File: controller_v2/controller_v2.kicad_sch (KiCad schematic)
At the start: 22 parts, among them J1 Conn_01x03_Socket, J2 WAGO 236-402, J3 WAGO 236-402, J4 WAGO 236-404, Q1 2N2222

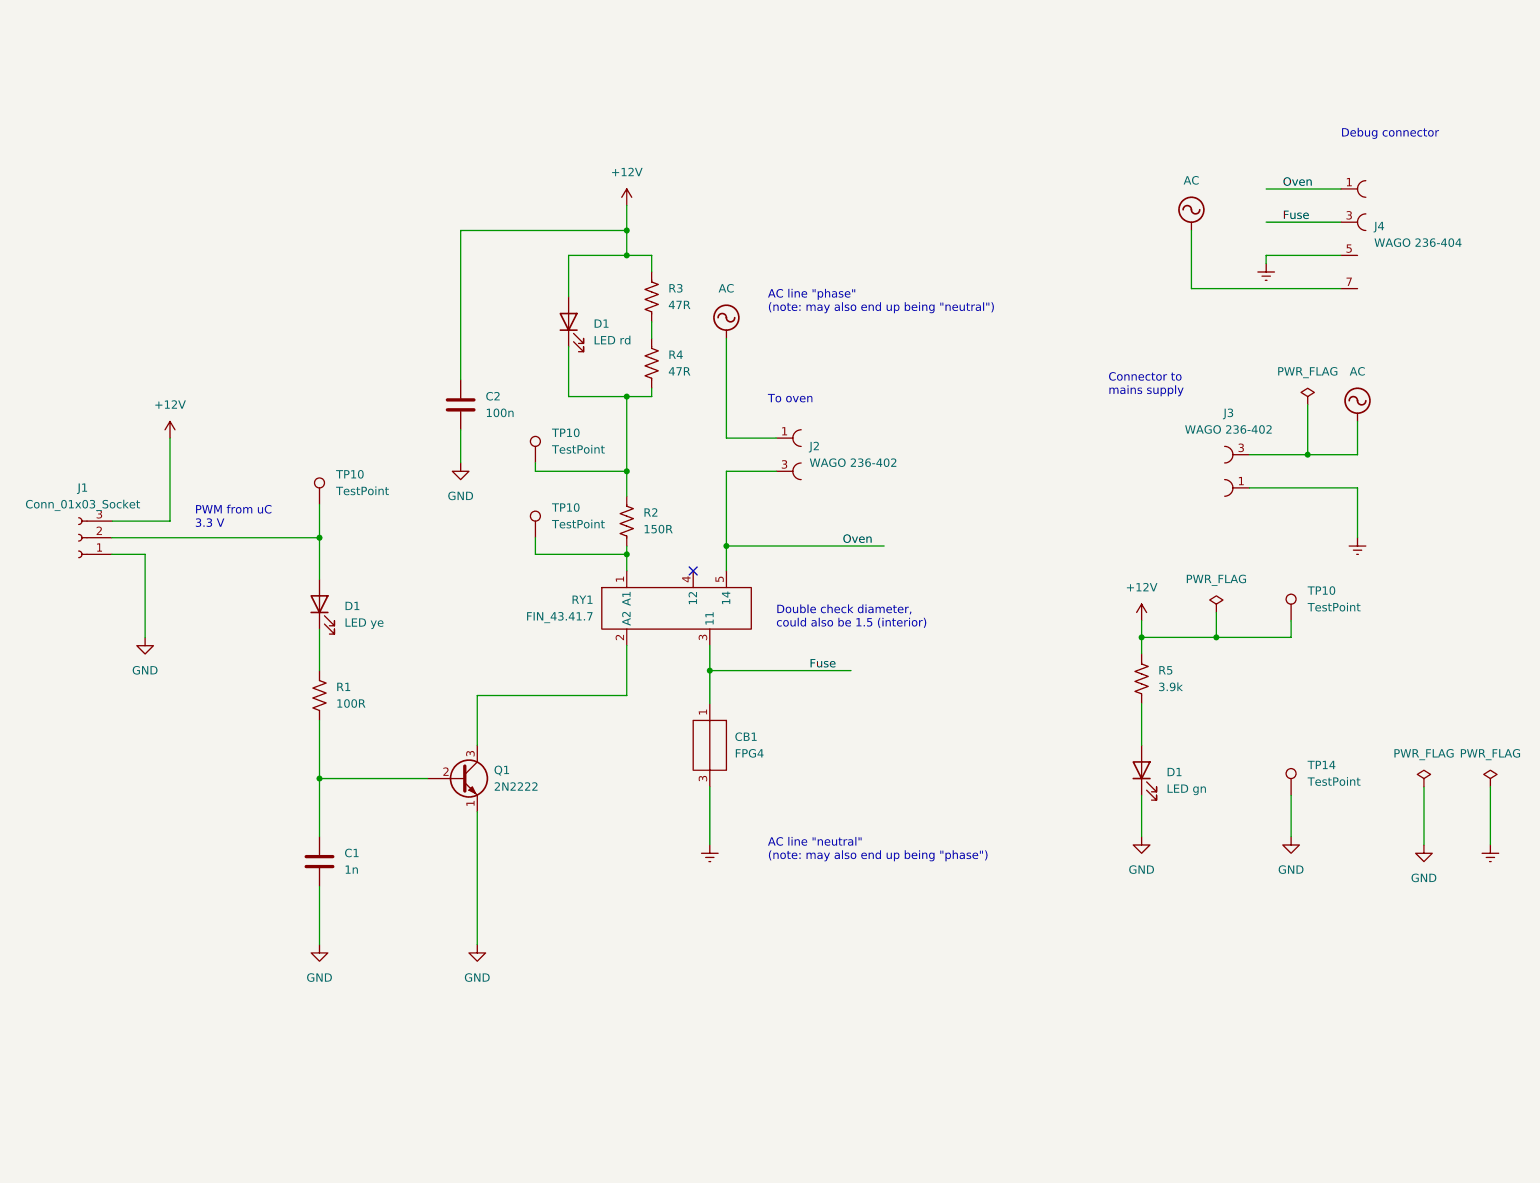
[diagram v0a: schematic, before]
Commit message: Added the schematic of the thermo sensor and the MCU
Not yet added the board itself.
Also, the MCU needs to be replaced by the SMD part.
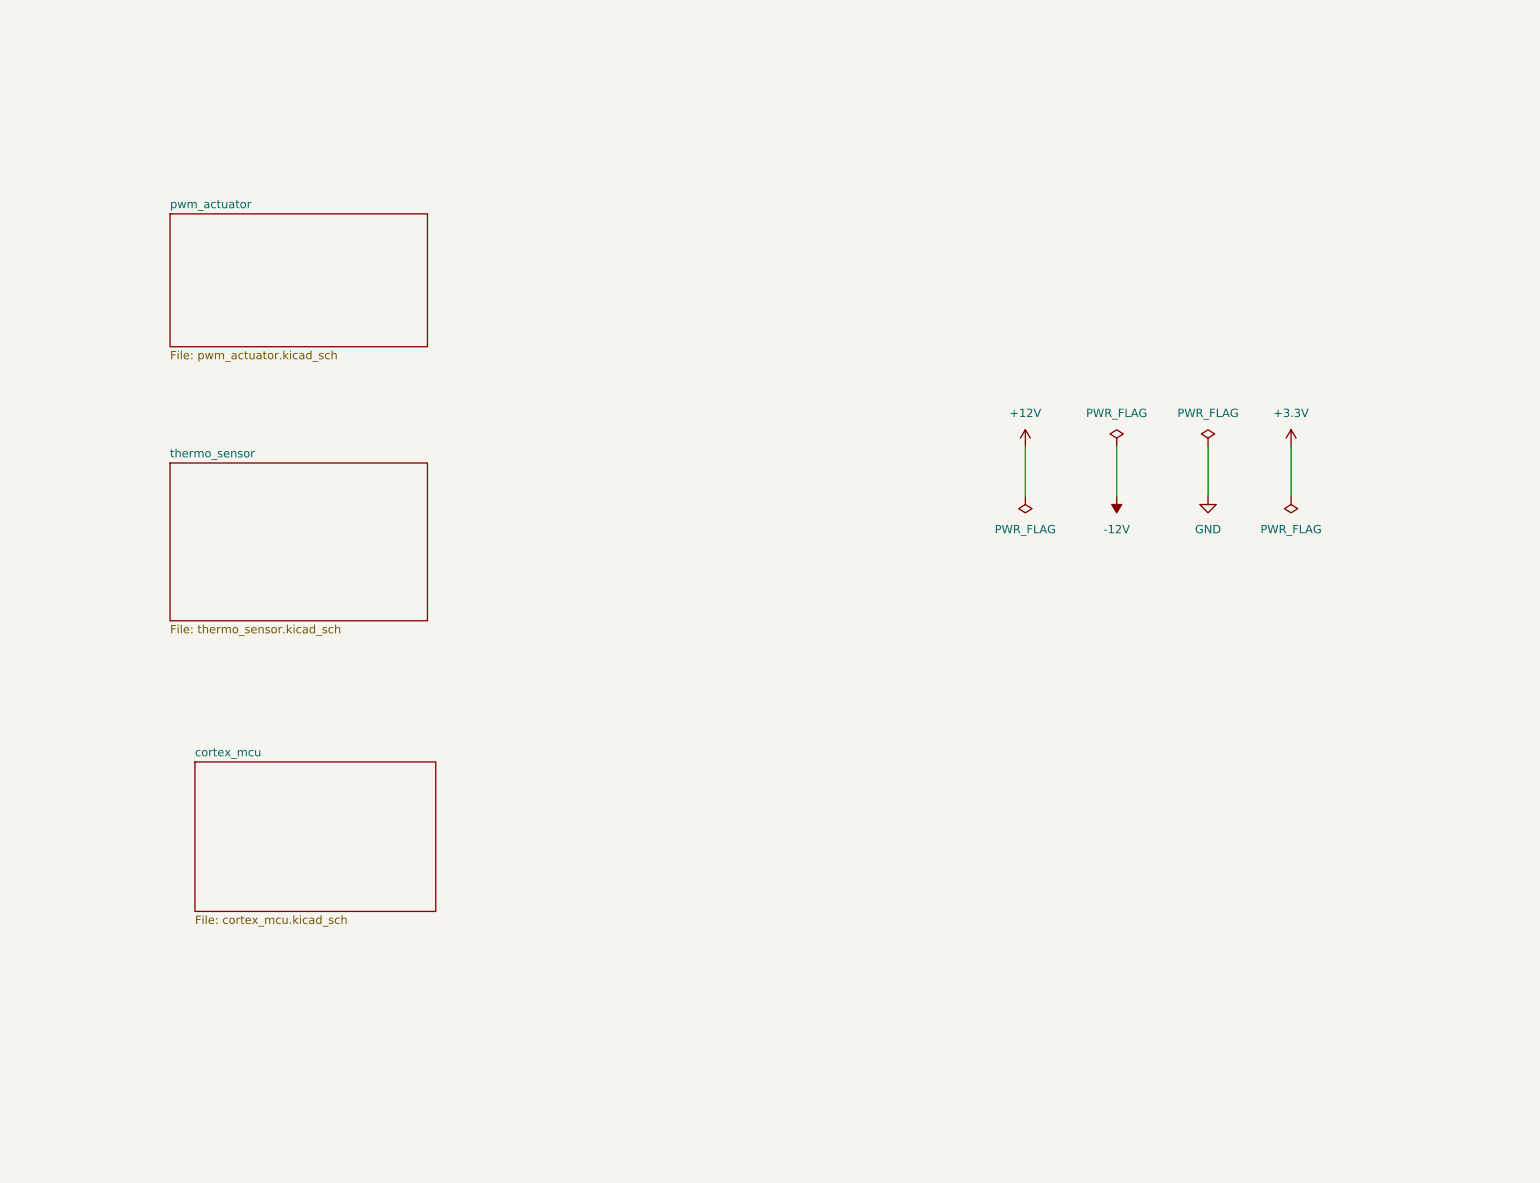
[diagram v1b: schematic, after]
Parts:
- removed C1: 1n, Capacitor_THT:C_Disc_D5.0mm_W2.5mm_P5.00mm, symbol Device:C
- removed C2: 100n, Capacitor_THT:C_Disc_D5.0mm_W2.5mm_P2.50mm, symbol Device:C
- removed CB1: FPG4, electrical:FPG4, symbol electrical:FPG4
- removed D1: LED rd, LED_THT:LED_D5.0mm, symbol Device:LED
- removed D1: LED gn, LED_THT:LED_D5.0mm, symbol Device:LED
- removed D1: LED ye, LED_THT:LED_D5.0mm, symbol Device:LED
- removed J1: Conn_01x03_Socket, Connector_PinSocket_2.54mm:PinSocket_1x03_P2.54mm_Vertical, symbol Connector:Conn_01x03_Socket
- removed J2, J3: WAGO 236-402, connectors:WAGO 236-402, symbol connectors:WAGO_236-402
- removed J4: WAGO 236-404, connectors:WAGO 236-404, symbol connectors:WAGO_236-404
- removed Q1: 2N2222, active:2N2222, symbol active:2N2222
- removed R1: 100R, Resistor_THT:R_Axial_DIN0207_L6.3mm_D2.5mm_P10.16mm_Horizontal, symbol Device:R_US
- removed R2: 150R, Resistor_THT:R_Axial_DIN0207_L6.3mm_D2.5mm_P10.16mm_Horizontal, symbol Device:R_US
- removed R3, R4: 47R, Resistor_THT:R_Axial_DIN0207_L6.3mm_D2.5mm_P10.16mm_Horizontal, symbol Device:R_US
- removed R5: 3.9k, Resistor_THT:R_Axial_DIN0207_L6.3mm_D2.5mm_P10.16mm_Horizontal, symbol Device:R_US
- removed RY1: FIN_43.41.7, electrical:FIN 43.41.7, symbol electrical:FIN_43.41.7
- removed TP10 (x4): TestPoint, TestPoint:TestPoint_Pad_2.0x2.0mm, symbol Connector:TestPoint
- removed TP14: TestPoint, TestPoint:TestPoint_Plated_Hole_D2.0mm, symbol Connector:TestPoint
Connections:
- no-connect marks 1 -> 0
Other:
- added sheet cortex_mcu (cortex_mcu.kicad_sch)
- added sheet pwm_actuator (pwm_actuator.kicad_sch)
- added sheet thermo_sensor (thermo_sensor.kicad_sch)
- note removed: "AC line "neutral" (note: may also end up being "phase")"
- note removed: "AC line "phase" (note: may also end up being "neutral")"
- note removed: "Connector to mains supply"
- note removed: "Debug connector"
- note removed: "Double check diameter, could also be 1.5 (interior)"
- note removed: "PWM from uC 3.3 V"
- note removed: "To oven"
- company: Philipp Rapp -> Dr. Philipp Rapp -- HydroSynapse signal processing
- title: Reflow oven controller board -> Reflow oven controller board version 2

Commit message: Cleanup schematic
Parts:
- added TP4, TP7: TestPoint, TestPoint:TestPoint_Plated_Hole_D2.0mm, symbol Connector:TestPoint
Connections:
- net GND: now also TP4.1, TP7.1
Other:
- sheet cortex_mcu ports: added PWM_FROM_UC, SCK, SO, ~{CS}; removed none
- sheet pwm_actuator ports: added PWM_FROM_UC; removed none
- sheet thermo_sensor ports: added SCK, SO, ~{CS}; removed none

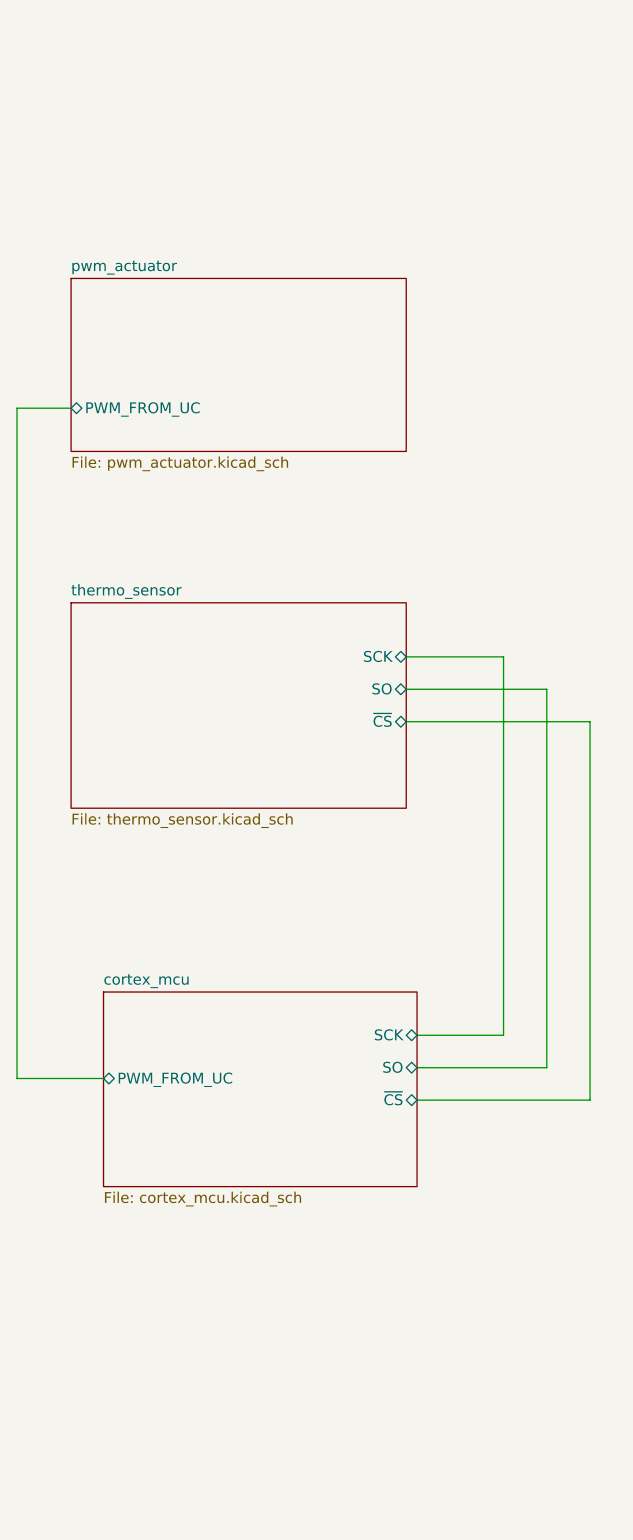
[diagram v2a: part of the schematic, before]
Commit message: Replaced Cortex MCU by SMD part
Removed the evaluation board. Inserted the SMD part.
Took over connections.
Added the hierarchical sheets power and mcu_power.

Only adapted the schematic, not the board.
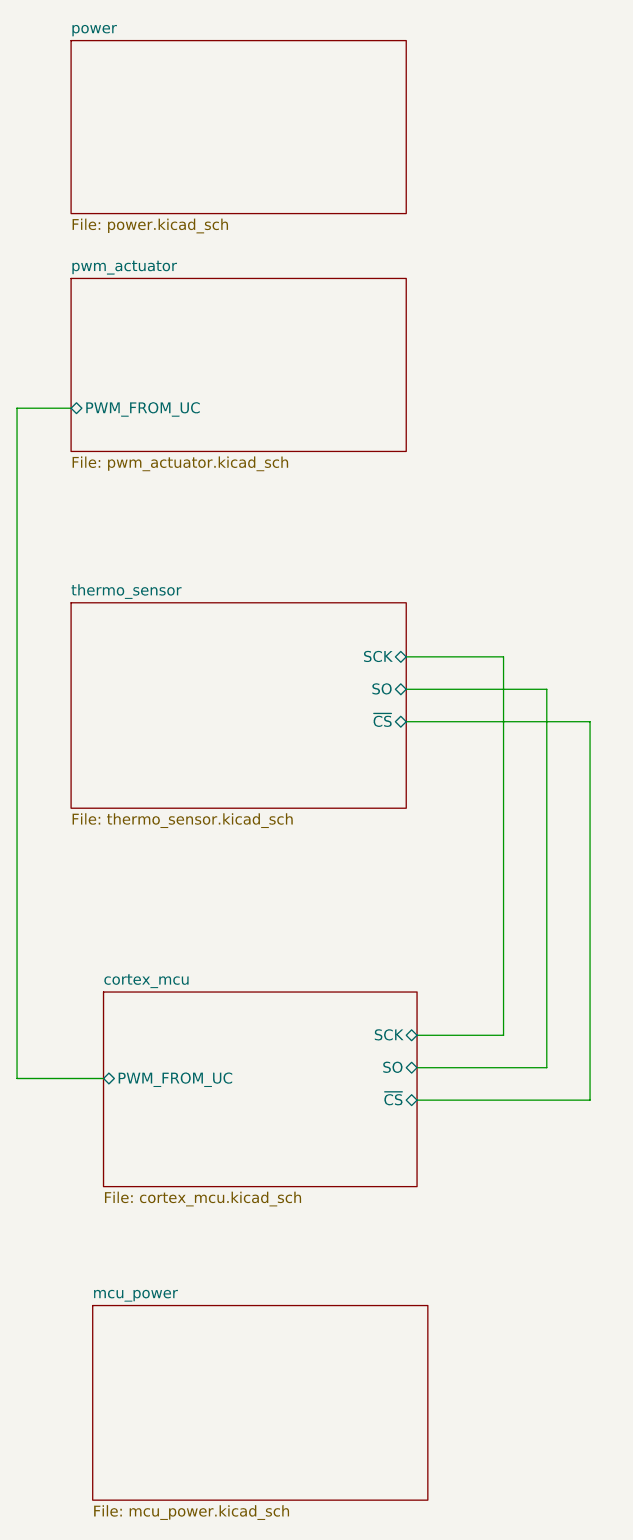
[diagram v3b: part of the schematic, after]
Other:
- added sheet mcu_power (mcu_power.kicad_sch)
- added sheet power (power.kicad_sch)
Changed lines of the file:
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@@
+    )
+  )
+  (sheet (at 50.8 16.51) (size 39.37 20.32) (fields_autoplaced)
+    (stroke (width 0.1524) (type solid))
+    (fill (color 0 0 0 0.0000))
+    (property "Sheetname" "power" (at 50.8 15.7984 0)
+      (effects (font (size 1.27 1.27)) (justify left bottom))
+    )
+    (property "Sheetfile" "power.kicad_sch" (at 50.8 37.4146 0)
+      (effects (font (size 1.27 1.27)) (justify left top))
+    )
+    (instances
+      (project "controller_v2"
+        (path "/884d8f78-75d7-4449-b027-2ba1bd4eeac8" (page "5"))
+      )
     )
   )
@@
       )
     )
+  )
+  (sheet (at 53.34 165.1) (size 39.37 22.86) (fields_autoplaced)
+    (stroke (width 0.1524) (type solid))
+    (fill (color 0 0 0 0.0000))
+    (property "Sheetname" "mcu_power" (at 53.34 164.3884 0)
+      (effects (font (size 1.27 1.27)) (justify left bottom))
+    )
+    (property "Sheetfile" "mcu_power.kicad_sch" (at 53.34 188.5446 0)
+      (effects (font (size 1.27 1.27)) (justify left top))
+    )
+    (instances
+      (project "controller_v2"
+        (path "/884d8f78-75d7-4449-b027-2ba1bd4eeac8" (page "6"))
+      )
+    )
